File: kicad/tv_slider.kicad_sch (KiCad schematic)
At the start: 1 part, among them U1 ESP32-C6-DEVKITC-1-N8

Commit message: top level schematic completed
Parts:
- removed U1: ESP32-C6-DEVKITC-1-N8, local_library:MODULE_ESP32-C6-DEVKITC-1-N8, symbol local_library:ESP32-C6-DEVKITC-1-N8
- added FID1, FID2, FID3: Fiducial, Fiducial:Fiducial_1mm_Mask2mm, symbol Mechanical:Fiducial
- added J1: Conn_01x02, TerminalBlock_RND:TerminalBlock_RND_205-00276_1x02_P5.00mm_Vertical, symbol Connector_Generic:Conn_01x02
- added J2: Conn_01x04, TerminalBlock_RND:TerminalBlock_RND_205-00278_1x04_P5.00mm_Vertical, symbol Connector_Generic:Conn_01x04
- added J3: Conn_01x06, TerminalBlock_RND:TerminalBlock_RND_205-00280_1x06_P5.00mm_Vertical, symbol Connector_Generic:Conn_01x06
- added J4, J5, J6, J7: Conn_01x03, TerminalBlock_RND:TerminalBlock_RND_205-00277_1x03_P5.00mm_Vertical, symbol Connector_Generic:Conn_01x03
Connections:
- new net +12V: J4.1 (Pin_1), J5.1 (Pin_1), J6.1 (Pin_1), J7.1 (Pin_1)
- new net +3.3V: J3.5 (Pin_5)
- new net GND: J1.2 (Pin_2), J3.6 (Pin_6), J4.3 (Pin_3), J5.3 (Pin_3), J6.3 (Pin_3), J7.3 (Pin_3)
- new net Location sensors/SENSOR_IN_SLOW: J6.2 (Pin_2)
- new net Location sensors/SENSOR_IN_STOP: J7.2 (Pin_2)
- new net Location sensors/SENSOR_OUT_SLOW: J5.2 (Pin_2)
- new net Location sensors/SENSOR_OUT_STOP: J4.2 (Pin_2)
- new net Motor drive/A+: J2.1 (Pin_1)
- new net Motor drive/A-: J2.2 (Pin_2)
- new net Motor drive/B+: J2.3 (Pin_3)
- new net Motor drive/B-: J2.4 (Pin_4)
- new net Power supply/Vin: J1.1 (Pin_1)
- new net Shaft encoder/A+: J3.3 (Pin_3)
- new net Shaft encoder/A-: J3.4 (Pin_4)
- new net Shaft encoder/B+: J3.1 (Pin_1)
- new net Shaft encoder/B-: J3.2 (Pin_2)
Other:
- added sheet Location sensors (location_sensors.kicad_sch)
- added sheet MCU (mcu.kicad_sch)
- added sheet Motor drive (motor_drive.kicad_sch)
- added sheet Power supply (power_supply.kicad_sch)
- added sheet Shaft encoder (shaft_encoder.kicad_sch)

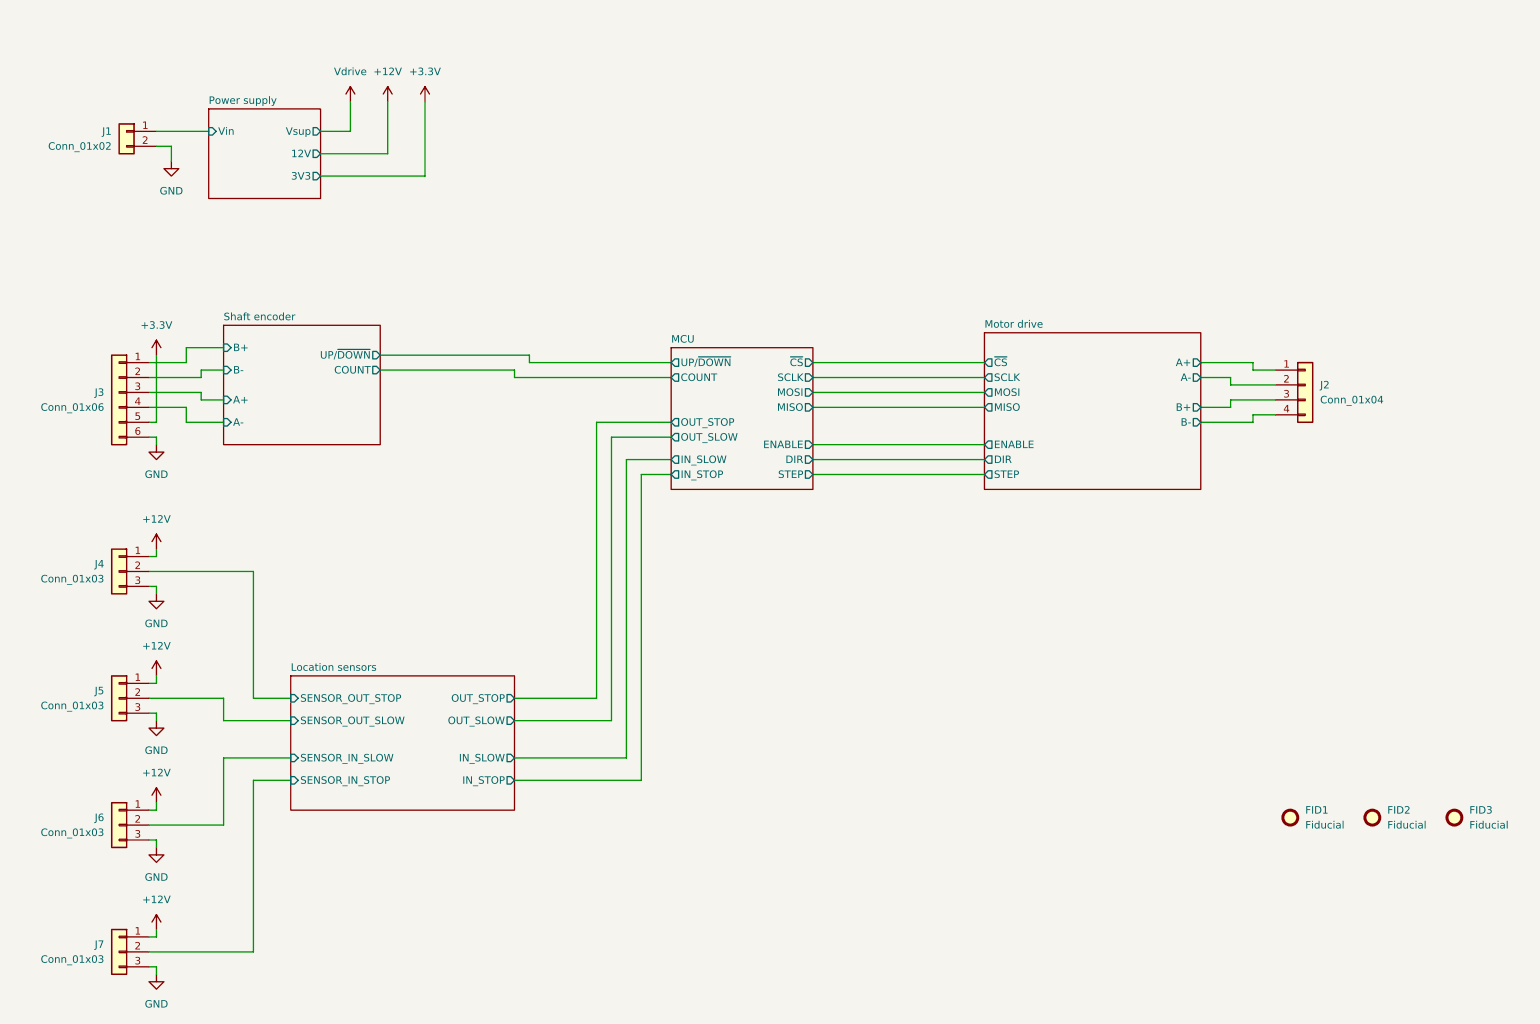
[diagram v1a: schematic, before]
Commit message: Completed the schematic. All components have Digikey part numbers and footprints. The power supply sheet still requires some work.
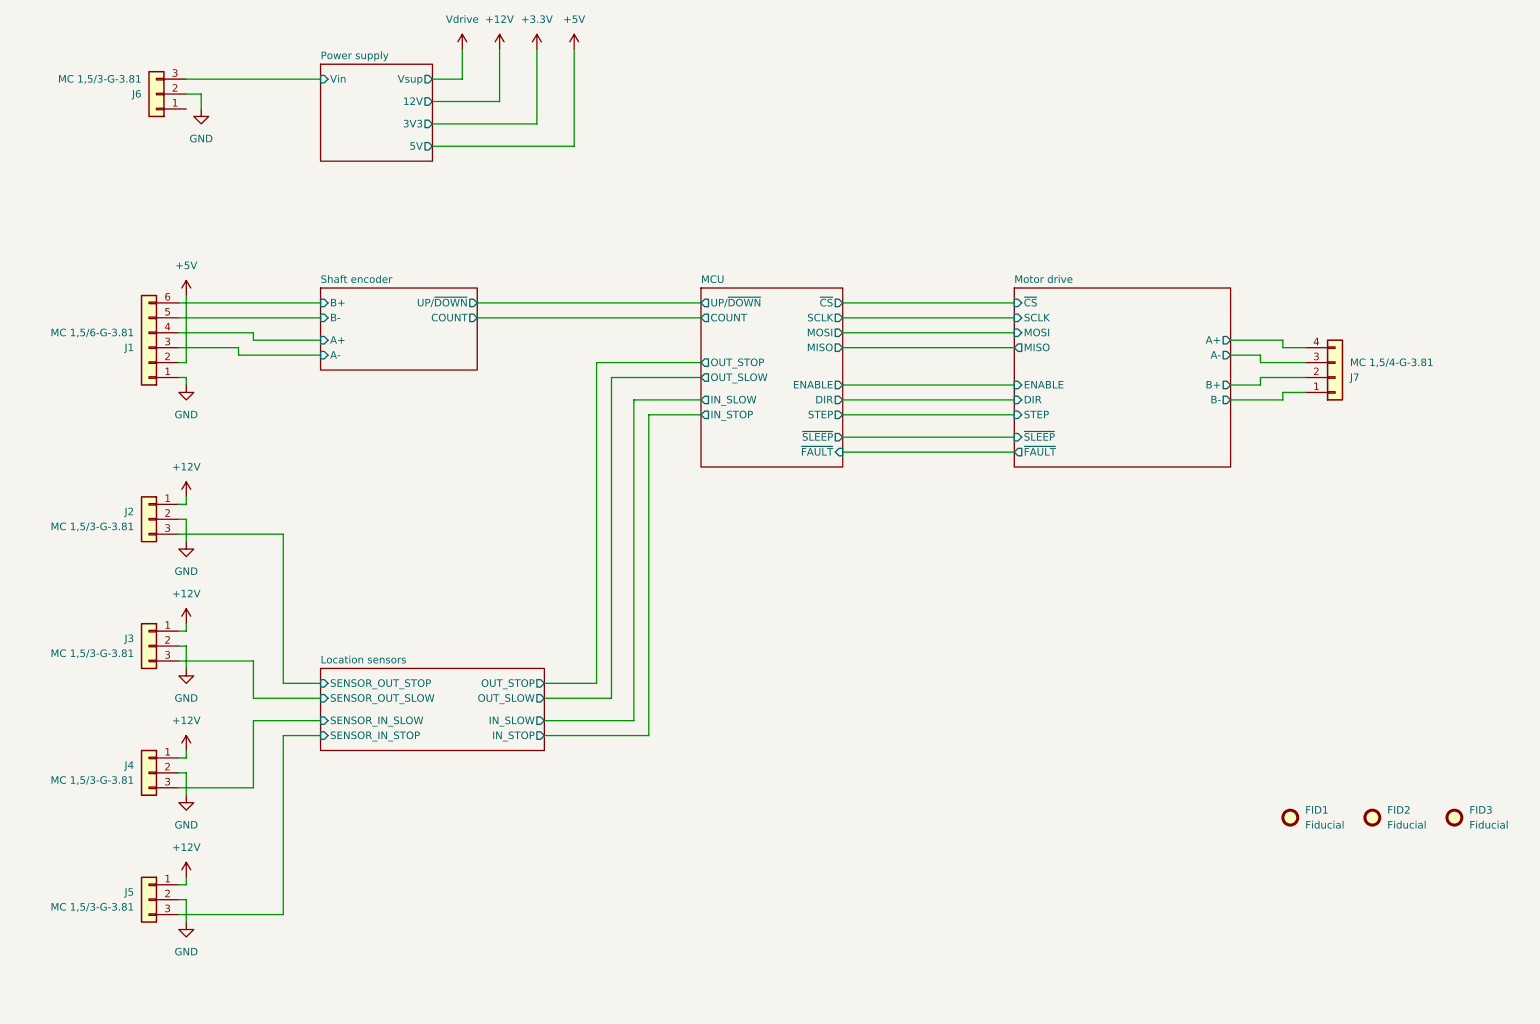
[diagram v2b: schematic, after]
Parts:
- J1: renamed from J3; value Conn_01x06 -> MC 1,5/6-G-3.81; footprint TerminalBlock_RND:TerminalBlock_RND_205-00280_1x06_P5.00mm_Vertical -> Connector_Phoenix_MC:PhoenixContact_MC_1,5_6-G-3.81_1x06_P3.81mm_Horizontal; MF (none) -> Phoenix; Supplier (none) -> Digi-Key; SupplierPN (none) -> 277-1210-ND
- J2: renamed from J4; value Conn_01x03 -> MC 1,5/3-G-3.81; footprint TerminalBlock_RND:TerminalBlock_RND_205-00277_1x03_P5.00mm_Vertical -> Connector_Phoenix_MC:PhoenixContact_MC_1,5_3-G-3.81_1x03_P3.81mm_Horizontal; MF (none) -> Phoenix; Supplier (none) -> Digi-Key; SupplierPN (none) -> 277-1207-ND
- J3: renamed from J5; value Conn_01x03 -> MC 1,5/3-G-3.81; footprint TerminalBlock_RND:TerminalBlock_RND_205-00277_1x03_P5.00mm_Vertical -> Connector_Phoenix_MC:PhoenixContact_MC_1,5_3-G-3.81_1x03_P3.81mm_Horizontal; MF (none) -> Phoenix; Supplier (none) -> Digi-Key; SupplierPN (none) -> 277-1207-ND
- J4: renamed from J6; value Conn_01x03 -> MC 1,5/3-G-3.81; footprint TerminalBlock_RND:TerminalBlock_RND_205-00277_1x03_P5.00mm_Vertical -> Connector_Phoenix_MC:PhoenixContact_MC_1,5_3-G-3.81_1x03_P3.81mm_Horizontal; MF (none) -> Phoenix; Supplier (none) -> Digi-Key; SupplierPN (none) -> 277-1207-ND
- J5: renamed from J7; value Conn_01x03 -> MC 1,5/3-G-3.81; footprint TerminalBlock_RND:TerminalBlock_RND_205-00277_1x03_P5.00mm_Vertical -> Connector_Phoenix_MC:PhoenixContact_MC_1,5_3-G-3.81_1x03_P3.81mm_Horizontal; MF (none) -> Phoenix; Supplier (none) -> Digi-Key; SupplierPN (none) -> 277-1207-ND
- J6: renamed from J1; value Conn_01x02 -> MC 1,5/3-G-3.81; footprint TerminalBlock_RND:TerminalBlock_RND_205-00276_1x02_P5.00mm_Vertical -> Connector_Phoenix_MC:PhoenixContact_MC_1,5_3-G-3.81_1x03_P3.81mm_Horizontal; symbol Connector_Generic:Conn_01x02 -> Connector_Generic:Conn_01x03; MF (none) -> Phoenix; Supplier (none) -> Digi-Key; SupplierPN (none) -> 277-1207-ND
- J7: renamed from J2; value Conn_01x04 -> MC 1,5/4-G-3.81; footprint TerminalBlock_RND:TerminalBlock_RND_205-00278_1x04_P5.00mm_Vertical -> Connector_Phoenix_MC:PhoenixContact_MC_1,5_4-G-3.81_1x04_P3.81mm_Horizontal; MF (none) -> Phoenix; Supplier (none) -> Digi-Key; SupplierPN (none) -> 277-1208-ND
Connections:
- net +3.3V: no longer J1.5 (Pin_5)
- net GND: now also J1.1 (Pin_1), J2.2 (Pin_2), J3.2 (Pin_2), J4.2 (Pin_2), J5.2 (Pin_2); no longer J1.6 (Pin_6), J2.3 (Pin_3), J3.3 (Pin_3), J4.3 (Pin_3), J5.3 (Pin_3)
- net Location sensors/SENSOR_IN_SLOW: now also J4.3 (Pin_3); no longer J4.2 (Pin_2)
- net Location sensors/SENSOR_IN_STOP: now also J5.3 (Pin_3); no longer J5.2 (Pin_2)
- net Location sensors/SENSOR_OUT_SLOW: now also J3.3 (Pin_3); no longer J3.2 (Pin_2)
- net Location sensors/SENSOR_OUT_STOP: now also J2.3 (Pin_3); no longer J2.2 (Pin_2)
- net Motor drive/A+: now also J7.4 (Pin_4); no longer J7.1 (Pin_1)
- net Motor drive/A-: now also J7.3 (Pin_3); no longer J7.2 (Pin_2)
- net Motor drive/B+: now also J7.2 (Pin_2); no longer J7.3 (Pin_3)
- net Motor drive/B-: now also J7.1 (Pin_1); no longer J7.4 (Pin_4)
- net Power supply/Vin: now also J6.3 (Pin_3); no longer J6.1 (Pin_1)
- net Shaft encoder/A+: now also J1.4 (Pin_4); no longer J1.3 (Pin_3)
- net Shaft encoder/A-: now also J1.3 (Pin_3); no longer J1.4 (Pin_4)
- net Shaft encoder/B+: now also J1.6 (Pin_6); no longer J1.1 (Pin_1)
- net Shaft encoder/B-: now also J1.5 (Pin_5); no longer J1.2 (Pin_2)
- new net +5V: J1.2 (Pin_2)
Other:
- sheet MCU ports: added ~{FAULT}, ~{SLEEP}; removed none
- sheet Motor drive ports: added ~{FAULT}, ~{SLEEP}; removed none
- sheet Power supply ports: added 5V; removed none
- company: (none) -> NX Solutions
- title: (none) -> TV slider
- moved on the sheet: J1, J2, J3, J4, J5, J7

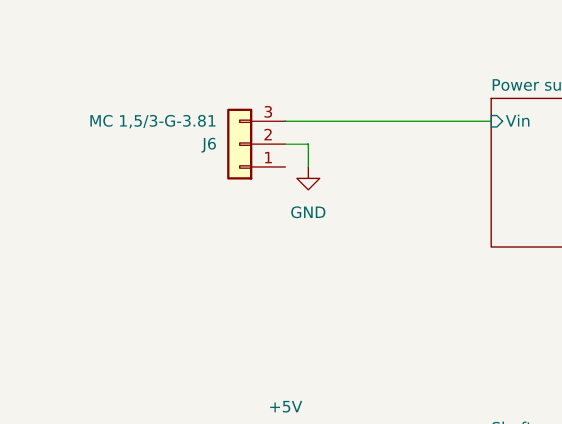
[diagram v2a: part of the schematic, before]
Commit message: Updated footprints and step models. Placed on PCB, but not yet positioned in final location.
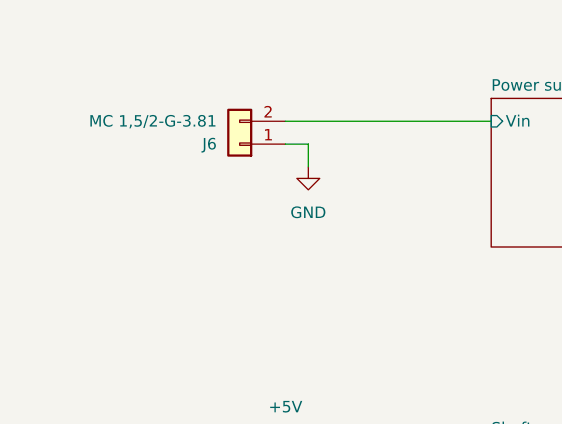
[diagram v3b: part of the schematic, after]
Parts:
- J6: value MC 1,5/3-G-3.81 -> MC 1,5/2-G-3.81; footprint Connector_Phoenix_MC:PhoenixContact_MC_1,5_3-G-3.81_1x03_P3.81mm_Horizontal -> Connector_Phoenix_MC:PhoenixContact_MC_1,5_2-G-3.81_1x02_P3.81mm_Horizontal; symbol Connector_Generic:Conn_01x03 -> Connector_Generic:Conn_01x02
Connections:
- net GND: now also J6.1 (Pin_1); no longer J6.2 (Pin_2)
- net Power supply/Vin: now also J6.2 (Pin_2); no longer J6.3 (Pin_3)
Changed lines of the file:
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@@
 		(dnp no)
 		(fields_autoplaced yes)
-		(property "Reference" "#PWR073"
+		(property "Reference" "#PWR015"
 			(at 119.38 34.29 0)
 			(effects
@@
 			(project ""
 				(path "/914c4b67-a7a4-47f3-8515-668040fd3f8c"
-					(reference "#PWR073")
+					(reference "#PWR015")
 					(unit 1)
 				)
@@
 	)
 	(symbol
-		(lib_id "Connector_Generic:Conn_01x03")
+		(lib_id "Connector_Generic:Conn_01x02")
 		(at 48.26 38.1 180)
 		(unit 1)
@@
 			)
 		)
-		(property "Value" "MC 1,5/3-G-3.81"
+		(property "Value" "MC 1,5/2-G-3.81"
 			(at 45.72 35.5601 0)
 			(effects
@@
 			)
 		)
-		(property "Footprint" "Connector_Phoenix_MC:PhoenixContact_MC_1,5_3-G-3.81_1x03_P3.81mm_Horizontal"
+		(property "Footprint" "Connector_Phoenix_MC:PhoenixContact_MC_1,5_2-G-3.81_1x02_P3.81mm_Horizontal"
 			(at 48.26 38.1 0)
 			(effects
@@
 			)
 		)
-		(property "Description" "Generic connector, single row, 01x03, script generated (kicad-library-utils/schlib/autogen/connector/)"
+		(property "Description" "Generic connector, single row, 01x02, script generated (kicad-library-utils/schlib/autogen/connector/)"
 			(at 48.26 38.1 0)
 			(effects
@@
 		(pin "2"
 		)
-		(pin "3"
-		)
-		(instances
+		(instances

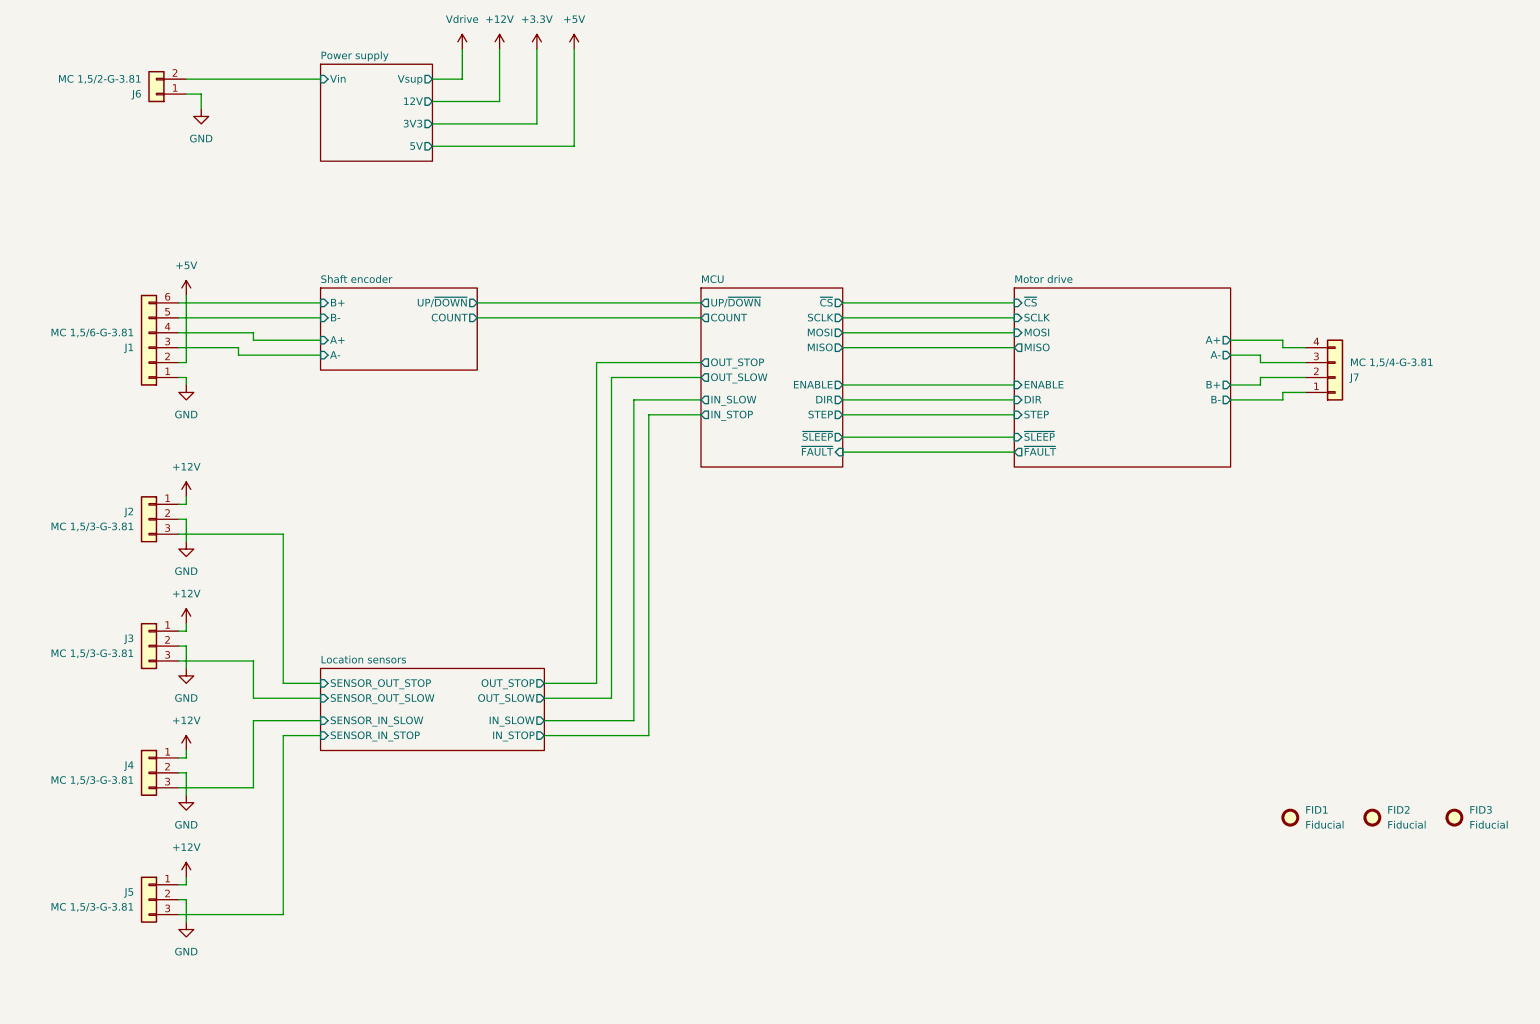
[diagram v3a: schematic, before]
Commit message: Updated all schematic pages except the power supply. Did the initial component placement.
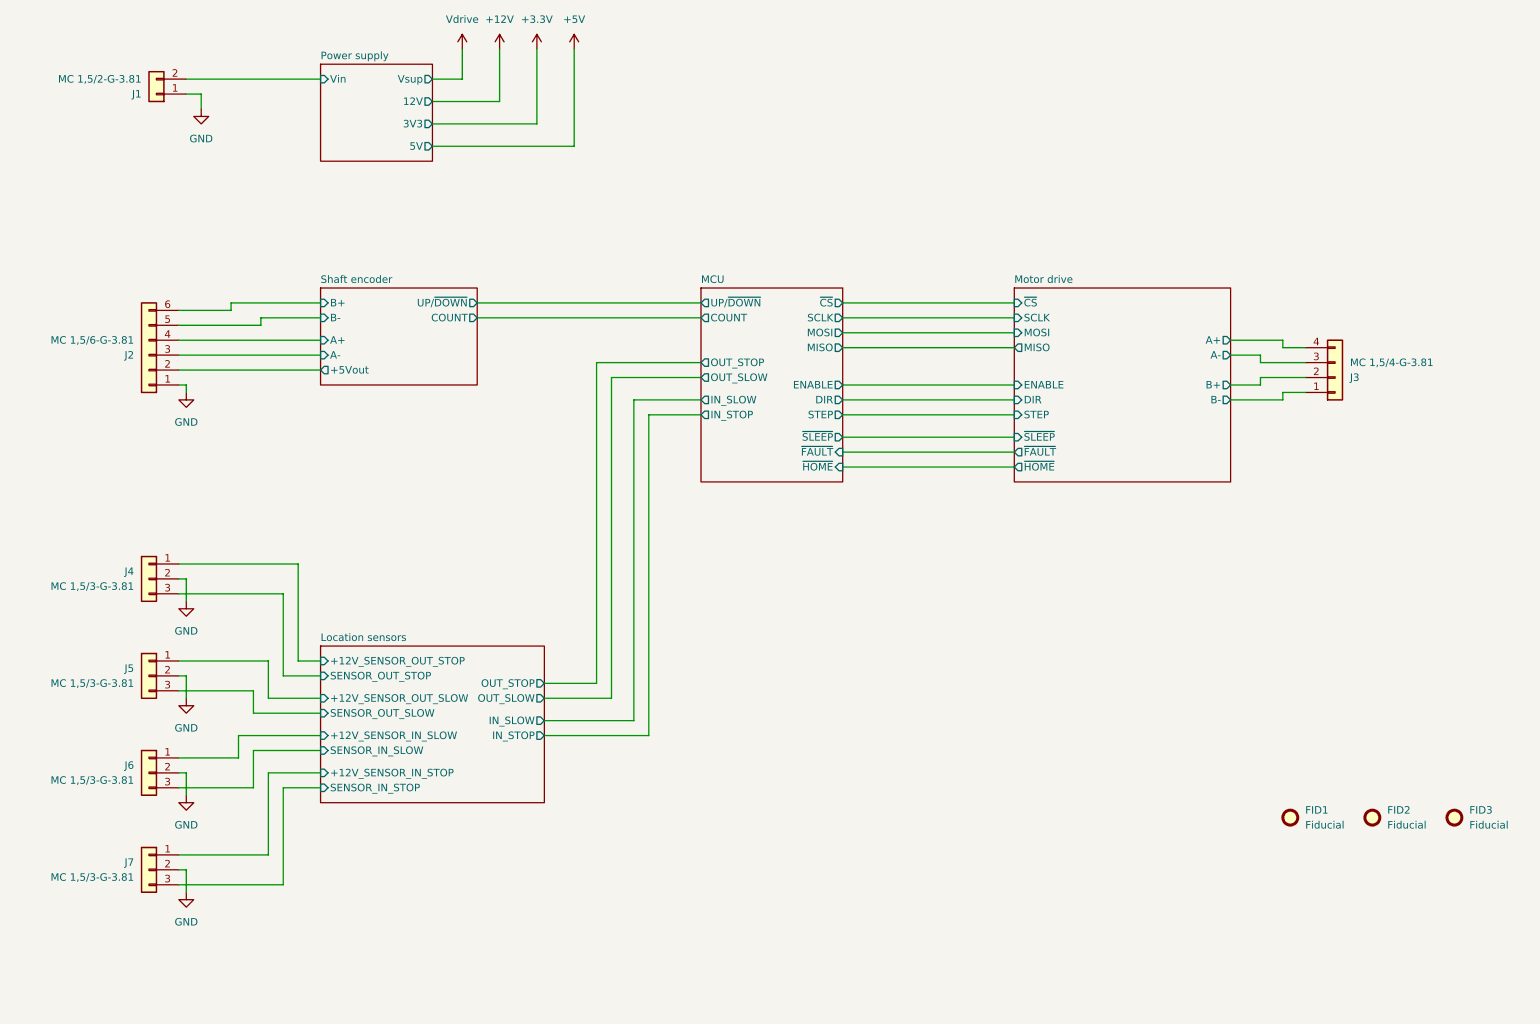
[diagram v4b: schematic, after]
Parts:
- renumbered J6 to J1, J1 to J2, J7 to J3, J2 to J4, J3 to J5, J4 to J6, J5 to J7
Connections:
- net +12V: no longer J4.1 (Pin_1), J5.1 (Pin_1), J6.1 (Pin_1), J7.1 (Pin_1)
- net +5V: no longer J2.2 (Pin_2)
- new net Location sensors/+12V_SENSOR_IN_SLOW: J6.1 (Pin_1)
- new net Location sensors/+12V_SENSOR_IN_STOP: J7.1 (Pin_1)
- new net Location sensors/+12V_SENSOR_OUT_SLOW: J5.1 (Pin_1)
- new net Location sensors/+12V_SENSOR_OUT_STOP: J4.1 (Pin_1)
- new net Shaft encoder/+5Vout: J2.2 (Pin_2)
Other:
- sheet Location sensors ports: added +12V_SENSOR_IN_SLOW, +12V_SENSOR_IN_STOP, +12V_SENSOR_OUT_SLOW, +12V_SENSOR_OUT_STOP; removed none
- sheet MCU ports: added ~{HOME}; removed none
- sheet Motor drive ports: added ~{HOME}; removed none
- sheet Shaft encoder ports: added +5Vout; removed none
- moved on the sheet: J2, J4, J5, J7
